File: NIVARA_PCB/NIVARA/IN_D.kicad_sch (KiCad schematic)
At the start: 0 parts

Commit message: avance
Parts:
- added C14, C15: C_0603, PCM_Capacitor_SMD_AKL:C_0603_1608Metric, symbol PCM_Capacitor_AKL:C_0603
- added LED10, LED9: LED_0603_Green, PCM_LED_SMD_AKL:LED_0603_1608Metric, symbol PCM_LED_AKL:LED_0603_Green
- added R36, R5: ?, PCM_Resistor_SMD_AKL:R_1206_3216Metric_Pad1.30x1.75mm_HandSolder, symbol PCM_Resistor_AKL:R_0603
- added R37, R38: 10K, PCM_Resistor_SMD_AKL:R_0603_1608Metric, symbol PCM_Resistor_AKL:R_0603
- added R39, R40: ?, PCM_Resistor_SMD_AKL:R_0603_1608Metric, symbol PCM_Resistor_AKL:R_0603
- added TP10, TP11: TestPoint, TestPoint:TestPoint_THTPad_D1.0mm_Drill0.5mm, symbol Connector:TestPoint
- added U3, U8: AT3H4A-CUH-S, easyeda2kicad:SSOP-4_L2.7-W4.6-P1.27-LS7.0-TL, symbol easyeda2kicad:AT3H4A-CUH-S
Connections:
- net IN_1: now also R5.2
- net OUT_1: now also C14.1, LED9.1 (K), R37.2, TP11.1, U3.4 (C)
- new net: R5.1, U3.1 (A/C)
- new net: R36.1, U8.1 (A/C)
- new net: LED10.2 (A), R40.2
- new net: LED9.2 (A), R39.2
- new net +3V3: R37.1, R38.1, R39.1, R40.1
- new net GND: C14.2, C15.2, U3.2 (C/A), U3.3 (E), U8.2 (C/A), U8.3 (E)
- new net IN_2: R36.2
- new net OUT_2: C15.1, LED10.1 (K), R38.2, TP10.1, U8.4 (C)

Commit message: SALIDAS DE VOLTAJE Y CORRIENTE
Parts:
- C14, C15: value C_0603 -> 1uF; PART NUMBERT (none) -> CL10A105KB8NNNC
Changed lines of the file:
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@@
 			)
 		)
-		(property "Value" "C_0603"
+		(property "Value" "1uF"
 			(at 100.33 72.3899 0)
 			(effects
@@
 			)
 		)
-		(property "PART NUMBERT" ""
+		(property "PART NUMBERT" "CL10A105KB8NNNC"
 			(at 96.52 71.12 0)
 			(effects
@@
 			)
 		)
-		(property "Value" "C_0603"
+		(property "Value" "1uF"
 			(at 100.33 120.6499 0)
 			(effects
@@
 			)
 		)
-		(property "PART NUMBERT" ""
+		(property "PART NUMBERT" "CL10A105KB8NNNC"
 			(at 96.52 119.38 0)
 			(effects

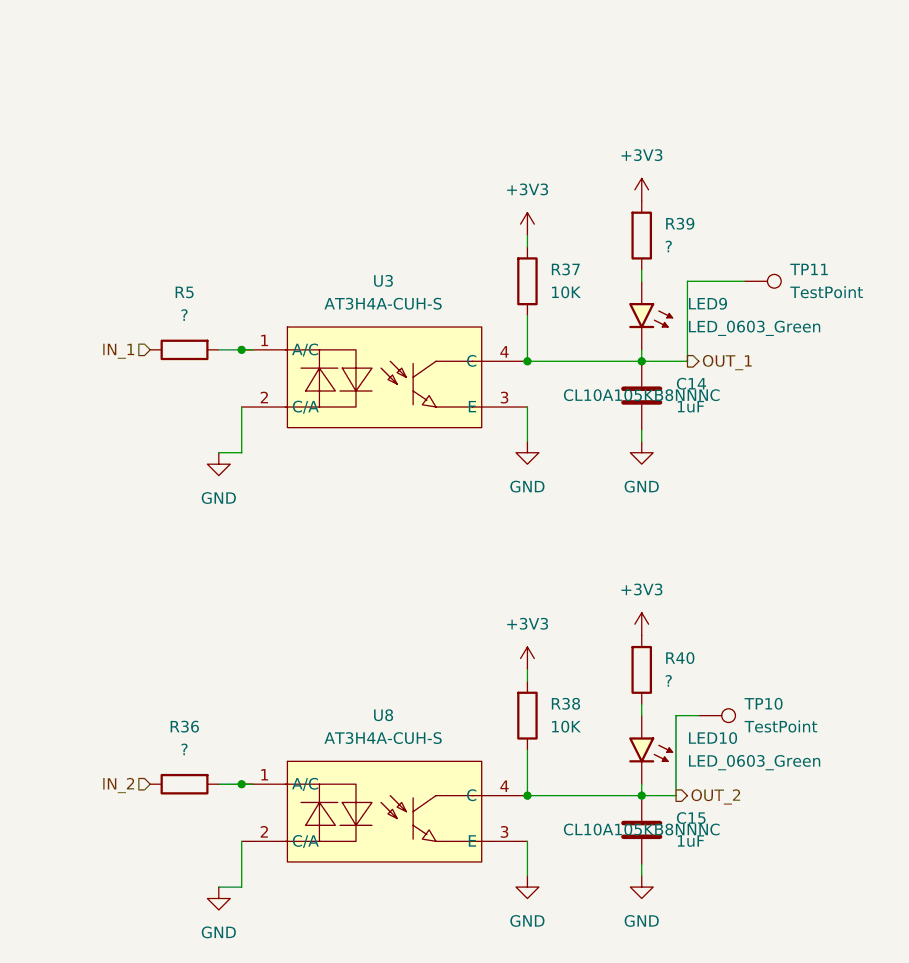
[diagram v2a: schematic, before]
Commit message: Se organizaron componentes en el area de PCB
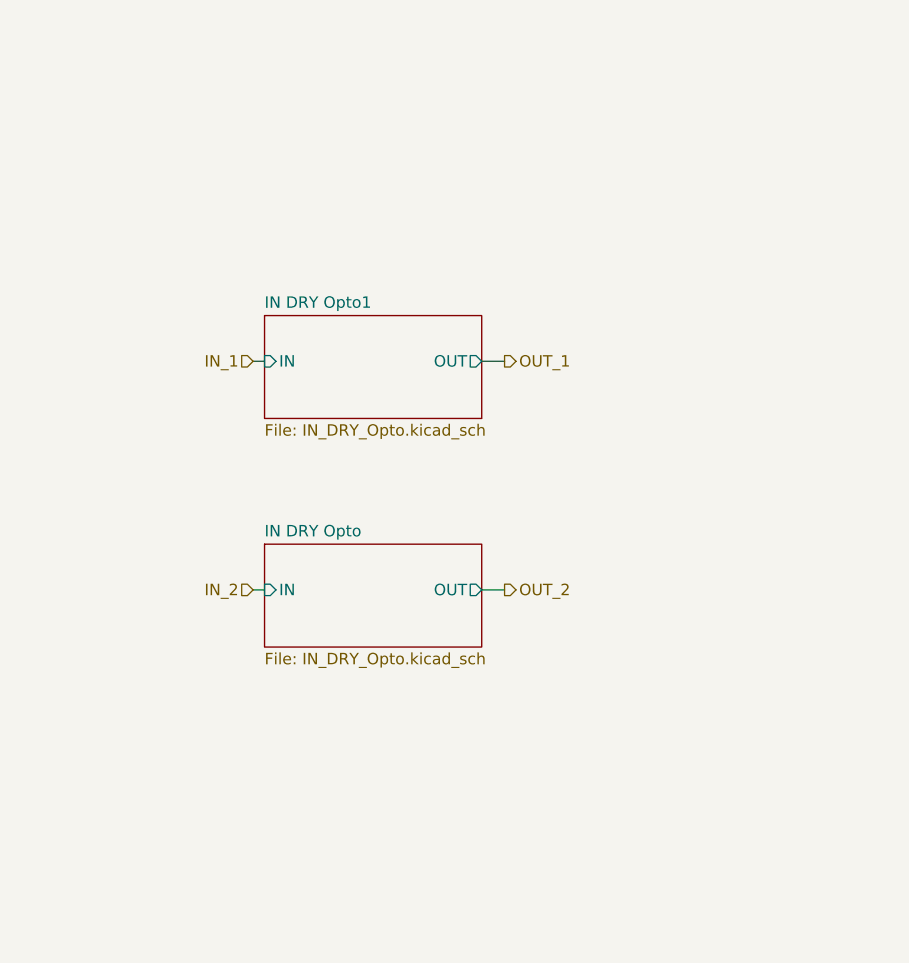
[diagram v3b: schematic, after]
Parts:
- removed C14, C15: 1uF, PCM_Capacitor_SMD_AKL:C_0603_1608Metric, symbol PCM_Capacitor_AKL:C_0603
- removed LED10, LED9: LED_0603_Green, PCM_LED_SMD_AKL:LED_0603_1608Metric, symbol PCM_LED_AKL:LED_0603_Green
- removed R36, R5: ?, PCM_Resistor_SMD_AKL:R_1206_3216Metric_Pad1.30x1.75mm_HandSolder, symbol PCM_Resistor_AKL:R_0603
- removed R37, R38: 10K, PCM_Resistor_SMD_AKL:R_0603_1608Metric, symbol PCM_Resistor_AKL:R_0603
- removed R39, R40: ?, PCM_Resistor_SMD_AKL:R_0603_1608Metric, symbol PCM_Resistor_AKL:R_0603
- removed TP10, TP11: TestPoint, TestPoint:TestPoint_THTPad_D1.0mm_Drill0.5mm, symbol Connector:TestPoint
- removed U3, U8: AT3H4A-CUH-S, easyeda2kicad:SSOP-4_L2.7-W4.6-P1.27-LS7.0-TL, symbol easyeda2kicad:AT3H4A-CUH-S
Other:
- added sheet IN DRY Opto (IN_DRY_Opto.kicad_sch)
- added sheet IN DRY Opto1 (IN_DRY_Opto.kicad_sch)
